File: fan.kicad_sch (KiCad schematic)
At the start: 11 parts, among them J4 Conn_01x04, U7 EMC2101

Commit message: added almost all of the feedback from NebulaMiner
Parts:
- added R?: 10K, Resistor_SMD:R_0402_1005Metric, symbol Device:R_US
- added R?: 19.3K, Resistor_SMD:R_0402_1005Metric, symbol Device:R_US
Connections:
- net FAN_TACH: now also R?.2
- net GND: now also R?.1
- new net ALERT: R?.1, R?.2
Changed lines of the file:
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@@
   (junction (at 113.665 78.105) (diameter 0) (color 0 0 0 0)
   )
+  (junction (at 74.295 108.585) (diameter 0) (color 0 0 0 0)
+  )
   (junction (at 191.77 66.04) (diameter 0) (color 0 0 0 0)
   )
@@
     (stroke (width 0) (type default) (color 0 0 0 0))
   )
+  (wire (pts (xy 74.295 105.41) (xy 74.295 108.585))
+    (stroke (width 0) (type default) (color 0 0 0 0))
+  )
   (wire (pts (xy 191.77 66.04) (xy 191.77 73.66))
     (stroke (width 0) (type default) (color 0 0 0 0))
@@
     (stroke (width 0) (type default) (color 0 0 0 0))
   )
+  (wire (pts (xy 74.295 108.585) (xy 74.295 111.125))
+    (stroke (width 0) (type default) (color 0 0 0 0))
+  )
   (wire (pts (xy 103.505 71.755) (xy 103.505 88.9))
     (stroke (width 0) (type default) (color 0 0 0 0))
@@
     (stroke (width 0) (type default) (color 0 0 0 0))
   )
+  (wire (pts (xy 67.31 108.585) (xy 74.295 108.585))
+    (stroke (width 0) (type default) (color 0 0 0 0))
+  )
   (wire (pts (xy 157.48 83.185) (xy 191.77 83.185))
     (stroke (width 0) (type default) (color 0 0 0 0))
@@
     (stroke (width 0) (type default) (color 0 0 0 0))
   )
+  (wire (pts (xy 74.295 97.79) (xy 74.295 94.615))
+    (stroke (width 0) (type default) (color 0 0 0 0))
+  )
   (wire (pts (xy 137.16 106.68) (xy 146.685 106.68))
     (stroke (width 0) (type default) (color 0 0 0 0))
@@
     (stroke (width 0) (type default) (color 0 0 0 0))
   )
+  (wire (pts (xy 74.295 94.615) (xy 85.725 94.615))
+    (stroke (width 0) (type default) (color 0 0 0 0))
+  )
+  (wire (pts (xy 74.295 118.745) (xy 74.295 127))
+    (stroke (width 0) (type default) (color 0 0 0 0))
+  )
   (text "I2C Address: 0x4C" (at 136.525 89.535 0)
     (effects (font (size 1.27 1.27)) (justify left bottom))
   )
+  (label "GND" (at 74.295 127 0)
+    (effects (font (size 1.27 1.27)) (justify left bottom))
+  )
   (label "FAN_PWM" (at 160.02 78.105 0)
     (effects (font (size 1.27 1.27)) (justify left bottom))
@@
   )
   (label "SDA" (at 162.56 75.565 0)
+    (effects (font (size 1.27 1.27)) (justify left bottom))
+  )
+  (label "FAN_TACH" (at 75.565 94.615 0)
     (effects (font (size 1.27 1.27)) (justify left bottom))
   )
@@
   )
   (hierarchical_label "TEMP_P" (shape input) (at 80.645 69.215 180)
+    (effects (font (size 1.27 1.27)) (justify right))
+  )
+  (hierarchical_label "ALERT" (shape input) (at 67.31 108.585 180)
     (effects (font (size 1.27 1.27)) (justify right))
   )
@@
     )
     (property "DK" "1292-1639-1-ND" (id 5) (at 191.77 78.74 0)
+      (effects (font (size 1.27 1.27)) hide)
+    )
+    (pin "1")
+    (pin "2")
+  )
+  (symbol (lib_id "Device:R_US") (at 74.295 101.6 180) (unit 1)
+    (in_bom yes) (on_board yes)
+    (property "Reference" "R?" (id 0) (at 77.47 100.965 0))
+    (property "Value" "10K" (id 1) (at 78.105 103.505 0))
+    (property "Footprint" "Resistor_SMD:R_0402_1005Metric" (id 2) (at 73.279 101.346 90)
+      (effects (font (size 1.27 1.27)) hide)
+    )
+    (property "Datasheet" "~" (id 3) (at 74.295 101.6 0)
+      (effects (font (size 1.27 1.27)) hide)
+    )
+    (property "DK" "YAG1346CT-ND" (id 4) (at 74.295 101.6 0)
       (effects (font (size 1.27 1.27)) hide)
     )
@@
     (pin "4")
   )
+  (symbol (lib_id "Device:R_US") (at 74.295 114.935 180) (unit 1)
+    (in_bom yes) (on_board yes)
+    (property "Reference" "R?" (id 0) (at 77.47 114.3 0))
+    (property "Value" "19.3K" (id 1) (at 79.375 116.84 0))
+    (property "Footprint" "Resistor_SMD:R_0402_1005Metric" (id 2) (at 73.279 114.681 90)
+      (effects (font (size 1.27 1.27)) hide)
+    )
+    (property "Datasheet" "~" (id 3) (at 74.295 114.935 0)
+      (effects (font (size 1.27 1.27)) hide)
+    )
+    (pin "1")
+    (pin "2")
+  )
   (symbol (lib_id "DayMiner-eagle-import:CAP0402") (at 113.665 84.455 0) (mirror y) (unit 1)

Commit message: part library cleanup
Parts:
- C32, C33: symbol DayMiner-eagle-import:CAP0402 -> Device:C
- gave numbers to parts that had none: 2
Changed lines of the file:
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@@
     (pin "1")
   )
-  (symbol (lib_id "DayMiner-eagle-import:CAP0402") (at 191.77 78.74 0) (mirror y) (unit 1)
+  (symbol (lib_id "Device:C") (at 191.77 77.47 0) (mirror y) (unit 1)
     (in_bom yes) (on_board yes)
     (property "Reference" "C33" (id 0) (at 196.215 76.2 0)
@@
       (effects (font (size 1.27 1.27)) (justify left bottom))
     )
-    (property "Footprint" "Capacitor_SMD:C_0402_1005Metric" (id 2) (at 191.77 78.74 0)
+    (property "Footprint" "Capacitor_SMD:C_0402_1005Metric" (id 2) (at 191.77 77.47 0)
       (effects (font (size 1.27 1.27)) hide)
     )
-    (property "Datasheet" "" (id 3) (at 191.77 78.74 0)
+    (property "Datasheet" "" (id 3) (at 191.77 77.47 0)
       (effects (font (size 1.27 1.27)) hide)
     )
-    (property "Value" "311-3342-1-ND" (id 4) (at 191.77 78.74 0)
+    (property "Value" "311-3342-1-ND" (id 4) (at 191.77 77.47 0)
       (effects (font (size 1.778 1.5113)) (justify left bottom) hide)
     )
-    (property "DK" "1292-1639-1-ND" (id 5) (at 191.77 78.74 0)
+    (property "DK" "1292-1639-1-ND" (id 5) (at 191.77 77.47 0)
       (effects (font (size 1.27 1.27)) hide)
     )
@@
   (symbol (lib_id "Device:R_US") (at 74.295 101.6 180) (unit 1)
     (in_bom yes) (on_board yes)
-    (property "Reference" "R?" (id 0) (at 77.47 100.965 0))
+    (property "Reference" "R24" (id 0) (at 77.47 100.965 0))
     (property "Value" "10K" (id 1) (at 78.105 103.505 0))
     (property "Footprint" "Resistor_SMD:R_0402_1005Metric" (id 2) (at 73.279 101.346 90)
@@
   (symbol (lib_id "Device:R_US") (at 74.295 114.935 180) (unit 1)
     (in_bom yes) (on_board yes)
-    (property "Reference" "R?" (id 0) (at 77.47 114.3 0))
+    (property "Reference" "R25" (id 0) (at 77.47 114.3 0))
     (property "Value" "19.3K" (id 1) (at 79.375 116.84 0))
     (property "Footprint" "Resistor_SMD:R_0402_1005Metric" (id 2) (at 73.279 114.681 90)
@@
     (pin "2")
   )
-  (symbol (lib_id "DayMiner-eagle-import:CAP0402") (at 113.665 84.455 0) (mirror y) (unit 1)
+  (symbol (lib_id "Device:C") (at 113.665 83.185 0) (mirror y) (unit 1)
     (in_bom yes) (on_board yes)
-    (property "Reference" "C32" (id 0) (at 112.141 81.534 0)
+    (property "Reference" "C32" (id 0) (at 113.03 81.28 0)
       (effects (font (size 1.27 1.27)) (justify left bottom))
     )
-    (property "Value" "470pF" (id 1) (at 112.141 86.614 0)
+    (property "Value" "470pF" (id 1) (at 113.03 86.36 0)
       (effects (font (size 1.27 1.27)) (justify left bottom))
     )
-    (property "Footprint" "Capacitor_SMD:C_0402_1005Metric" (id 2) (at 113.665 84.455 0)
+    (property "Footprint" "Capacitor_SMD:C_0402_1005Metric" (id 2) (at 113.665 83.185 0)
       (effects (font (size 1.27 1.27)) hide)
     )
-    (property "Datasheet" "" (id 3) (at 113.665 84.455 0)
+    (property "Datasheet" "" (id 3) (at 113.665 83.185 0)
       (effects (font (size 1.27 1.27)) hide)
     )
-    (property "DK" "" (id 4) (at 113.665 84.455 0)
+    (property "DK" "" (id 4) (at 113.665 83.185 0)
       (effects (font (size 1.778 1.5113)) (justify left bottom) hide)
     )

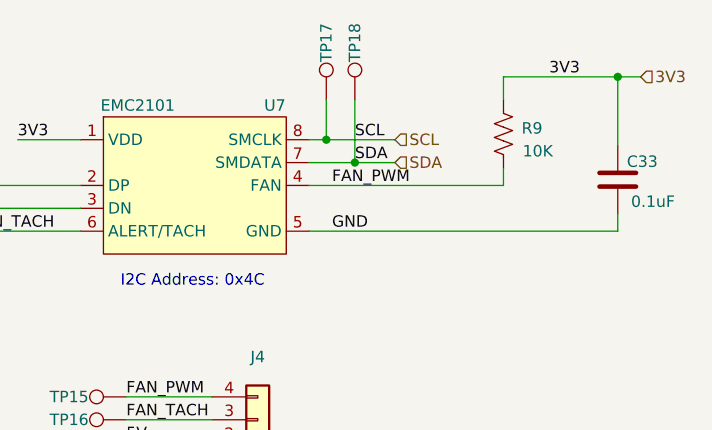
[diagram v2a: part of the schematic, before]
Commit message: more routing. fixed SDA/SCL short
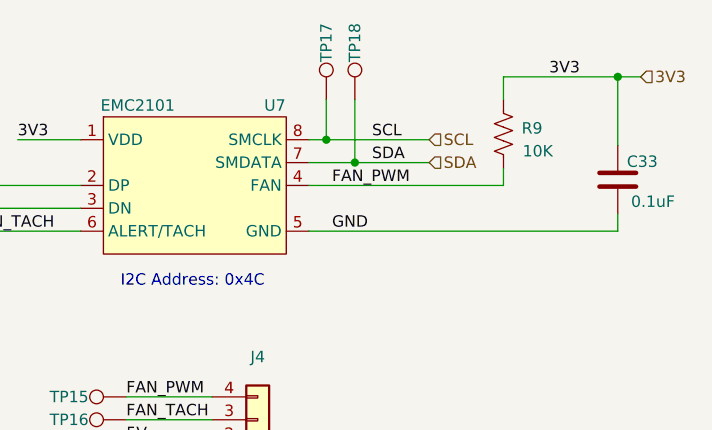
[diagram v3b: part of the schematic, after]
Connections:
- net SCL: no longer TP18.1, U7.7 (SMDATA)
- new net SDA: TP18.1, U7.7 (SMDATA)
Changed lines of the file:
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@@
     (stroke (width 0) (type default) (color 0 0 0 0))
   )
-  (wire (pts (xy 162.56 75.565) (xy 167.005 75.565))
+  (wire (pts (xy 162.56 75.565) (xy 170.815 75.565))
     (stroke (width 0) (type default) (color 0 0 0 0))
   )
@@
     (stroke (width 0) (type default) (color 0 0 0 0))
   )
-  (wire (pts (xy 159.385 73.025) (xy 167.005 73.025))
+  (wire (pts (xy 159.385 73.025) (xy 170.815 73.025))
     (stroke (width 0) (type default) (color 0 0 0 0))
   )
@@
     (effects (font (size 1.27 1.27)) (justify left bottom))
   )
-  (label "SCL" (at 162.56 73.025 0)
+  (label "SCL" (at 164.465 73.025 0)
     (effects (font (size 1.27 1.27)) (justify left bottom))
   )
@@
     (effects (font (size 1.27 1.27)) (justify left bottom))
   )
-  (label "SDA" (at 162.56 75.565 0)
+  (label "SDA" (at 164.465 75.565 0)
     (effects (font (size 1.27 1.27)) (justify left bottom))
   )
@@
     (effects (font (size 1.27 1.27)) (justify right))
   )
-  (hierarchical_label "SCL" (shape input) (at 167.005 73.025 0)
+  (hierarchical_label "SCL" (shape input) (at 170.815 73.025 0)
     (effects (font (size 1.27 1.27)) (justify left))
   )
@@
     (effects (font (size 1.27 1.27)) (justify right))
   )
-  (hierarchical_label "SDA" (shape input) (at 167.005 75.565 0)
+  (hierarchical_label "SDA" (shape input) (at 170.815 75.565 0)
     (effects (font (size 1.27 1.27)) (justify left))
   )

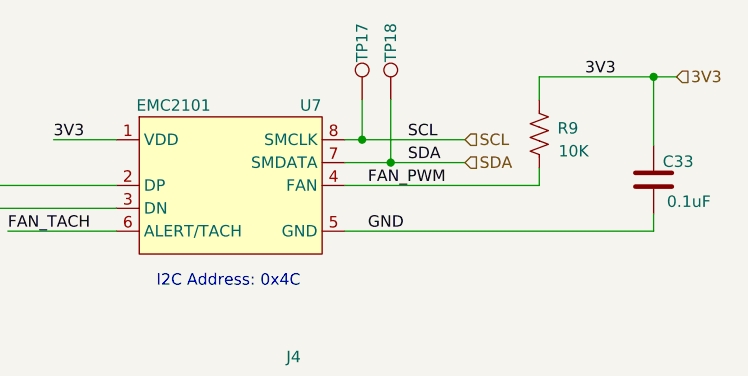
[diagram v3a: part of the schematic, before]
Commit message: lots of signals routed. much better ESP32-S3 3D model
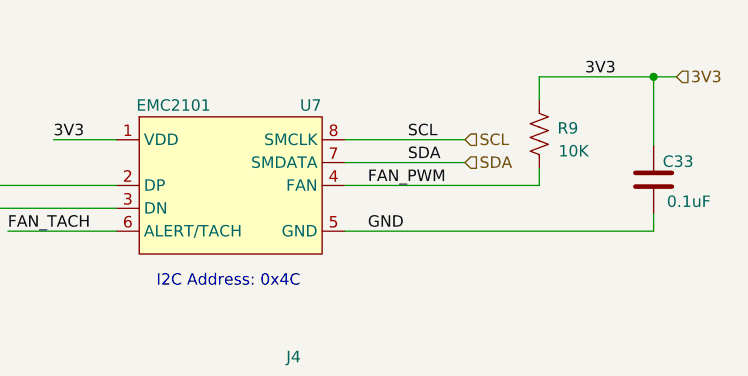
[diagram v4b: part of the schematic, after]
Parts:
- removed TP17, TP18: TestPoint, TestPoint:TestPoint_Pad_D1.5mm, symbol Connector:TestPoint
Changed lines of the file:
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@@
 (kicad_sch (version 20211123) (generator eeschema)
   (paper "A4")
-  (junction (at 162.56 75.565) (diameter 0) (color 0 0 0 0)
-  )
   (junction (at 113.665 78.105) (diameter 0) (color 0 0 0 0)
   )
@@
   (junction (at 191.77 66.04) (diameter 0) (color 0 0 0 0)
   )
-  (junction (at 159.385 73.025) (diameter 0) (color 0 0 0 0)
-  )
   (junction (at 113.665 88.9) (diameter 0) (color 0 0 0 0)
   )
-  (wire (pts (xy 157.48 73.025) (xy 159.385 73.025))
-    (stroke (width 0) (type default) (color 0 0 0 0))
-  )
-  (wire (pts (xy 159.385 68.58) (xy 159.385 73.025))
+  (wire (pts (xy 157.48 73.025) (xy 170.815 73.025))
     (stroke (width 0) (type default) (color 0 0 0 0))
   )
@@
     (stroke (width 0) (type default) (color 0 0 0 0))
   )
-  (wire (pts (xy 162.56 68.58) (xy 162.56 75.565))
-    (stroke (width 0) (type default) (color 0 0 0 0))
-  )
   (wire (pts (xy 80.645 71.755) (xy 92.075 71.755))
     (stroke (width 0) (type default) (color 0 0 0 0))
@@
     (stroke (width 0) (type default) (color 0 0 0 0))
   )
-  (wire (pts (xy 162.56 75.565) (xy 170.815 75.565))
+  (wire (pts (xy 157.48 75.565) (xy 170.815 75.565))
     (stroke (width 0) (type default) (color 0 0 0 0))
   )
@@
     (stroke (width 0) (type default) (color 0 0 0 0))
   )
-  (wire (pts (xy 159.385 73.025) (xy 170.815 73.025))
-    (stroke (width 0) (type default) (color 0 0 0 0))
-  )
   (wire (pts (xy 74.295 105.41) (xy 74.295 108.585))
     (stroke (width 0) (type default) (color 0 0 0 0))
@@
   )
   (wire (pts (xy 157.48 83.185) (xy 191.77 83.185))
-    (stroke (width 0) (type default) (color 0 0 0 0))
-  )
-  (wire (pts (xy 157.48 75.565) (xy 162.56 75.565))
     (stroke (width 0) (type default) (color 0 0 0 0))
   )
@@
     (pin "1")
     (pin "2")
-  )
-  (symbol (lib_id "Connector:TestPoint") (at 162.56 68.58 0) (mirror y) (unit 1)
-    (in_bom yes) (on_board yes)
-    (property "Reference" "TP18" (id 0) (at 162.56 62.23 90))
-    (property "Value" "TestPoint" (id 1) (at 161.2901 62.865 90)
-      (effects (font (size 1.27 1.27)) (justify left) hide)
-    )
-    (property "Footprint" "TestPoint:TestPoint_Pad_D1.5mm" (id 2) (at 157.48 68.58 0)
-      (effects (font (size 1.27 1.27)) hide)
-    )
-    (property "Datasheet" "~" (id 3) (at 157.48 68.58 0)
-      (effects (font (size 1.27 1.27)) hide)
-    )
-    (property "DNP" "T" (id 4) (at 162.56 68.58 0)
-      (effects (font (size 1.27 1.27)) hide)
-    )
-    (pin "1")
   )
   (symbol (lib_id "Connector_Generic:Conn_01x04") (at 151.765 106.68 0) (mirror x) (unit 1)
@@
     (pin "2")
   )
-  (symbol (lib_id "Connector:TestPoint") (at 159.385 68.58 0) (mirror y) (unit 1)
-    (in_bom yes) (on_board yes)
-    (property "Reference" "TP17" (id 0) (at 159.385 62.23 90))
-    (property "Value" "TestPoint" (id 1) (at 158.1151 62.865 90)
-      (effects (font (size 1.27 1.27)) (justify left) hide)
-    )
-    (property "Footprint" "TestPoint:TestPoint_Pad_D1.5mm" (id 2) (at 154.305 68.58 0)
-      (effects (font (size 1.27 1.27)) hide)
-    )
-    (property "Datasheet" "~" (id 3) (at 154.305 68.58 0)
-      (effects (font (size 1.27 1.27)) hide)
-    )
-    (property "DNP" "T" (id 4) (at 159.385 68.58 0)
-      (effects (font (size 1.27 1.27)) hide)
-    )
-    (pin "1")
-  )
   (symbol (lib_id "Device:R_US") (at 179.07 72.39 180) (unit 1)

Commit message: some DRC and BOM work
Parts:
- C32: DK (none) -> 1276-1566-1-ND
- R25: value 19.3K -> 19.1K; DK (none) -> YAG3027CT-ND
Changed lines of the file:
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@@
       (effects (font (size 1.27 1.27)) hide)
     )
-    (property "Datasheet" "" (id 3) (at 97.79 69.215 0)
+    (property "Datasheet" "~" (id 3) (at 97.79 69.215 0)
       (effects (font (size 1.27 1.27)) hide)
     )
@@
     (in_bom yes) (on_board yes)
     (property "Reference" "R25" (id 0) (at 77.47 114.3 0))
-    (property "Value" "19.3K" (id 1) (at 79.375 116.84 0))
+    (property "Value" "19.1K" (id 1) (at 79.375 116.84 0))
     (property "Footprint" "Resistor_SMD:R_0402_1005Metric" (id 2) (at 73.279 114.681 90)
       (effects (font (size 1.27 1.27)) hide)
     )
     (property "Datasheet" "~" (id 3) (at 74.295 114.935 0)
+      (effects (font (size 1.27 1.27)) hide)
+    )
+    (property "DK" "YAG3027CT-ND" (id 4) (at 74.295 114.935 0)
       (effects (font (size 1.27 1.27)) hide)
     )
@@
       (effects (font (size 1.27 1.27)) hide)
     )
-    (property "DK" "" (id 4) (at 113.665 83.185 0)
+    (property "DK" "1276-1566-1-ND" (id 4) (at 113.665 83.185 0)
       (effects (font (size 1.778 1.5113)) (justify left bottom) hide)
     )
@@
       (effects (font (size 1.27 1.27)) hide)
     )
-    (property "Datasheet" "" (id 3) (at 97.155 71.755 0)
+    (property "Datasheet" "~" (id 3) (at 97.155 71.755 0)
       (effects (font (size 1.27 1.27)) hide)
     )

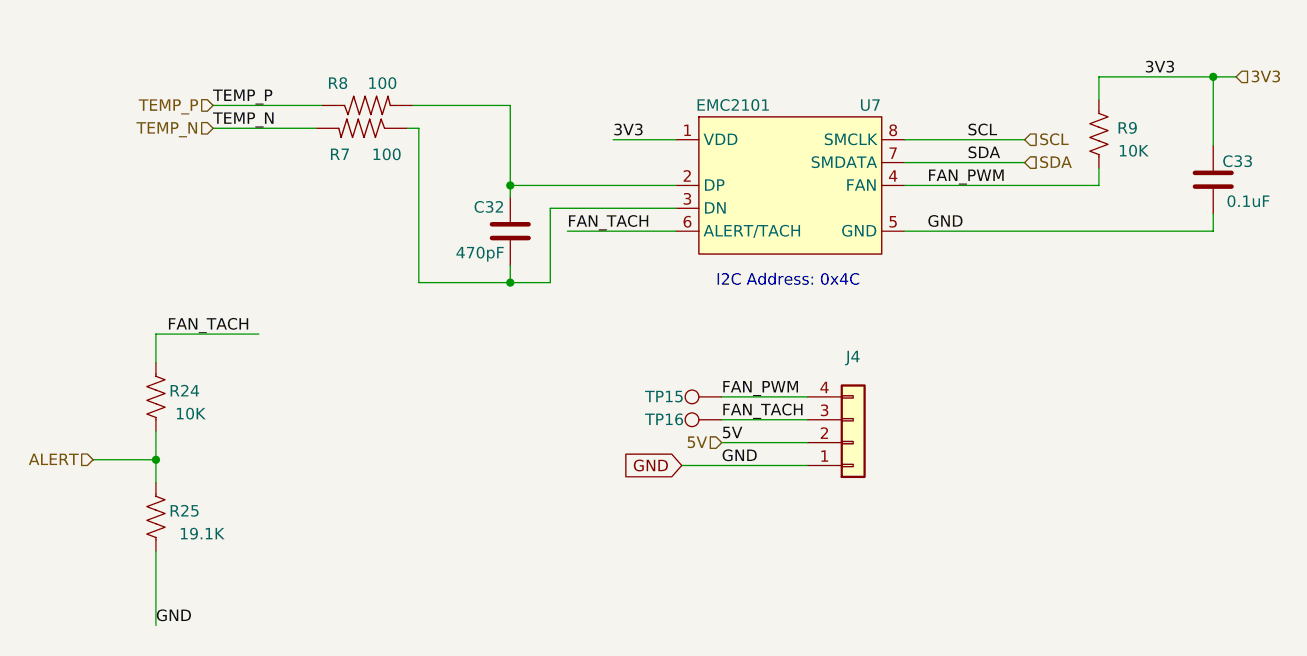
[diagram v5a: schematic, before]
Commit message: sorted out the resistor values for the DS4432. added some power filtering for the fan. created BOM
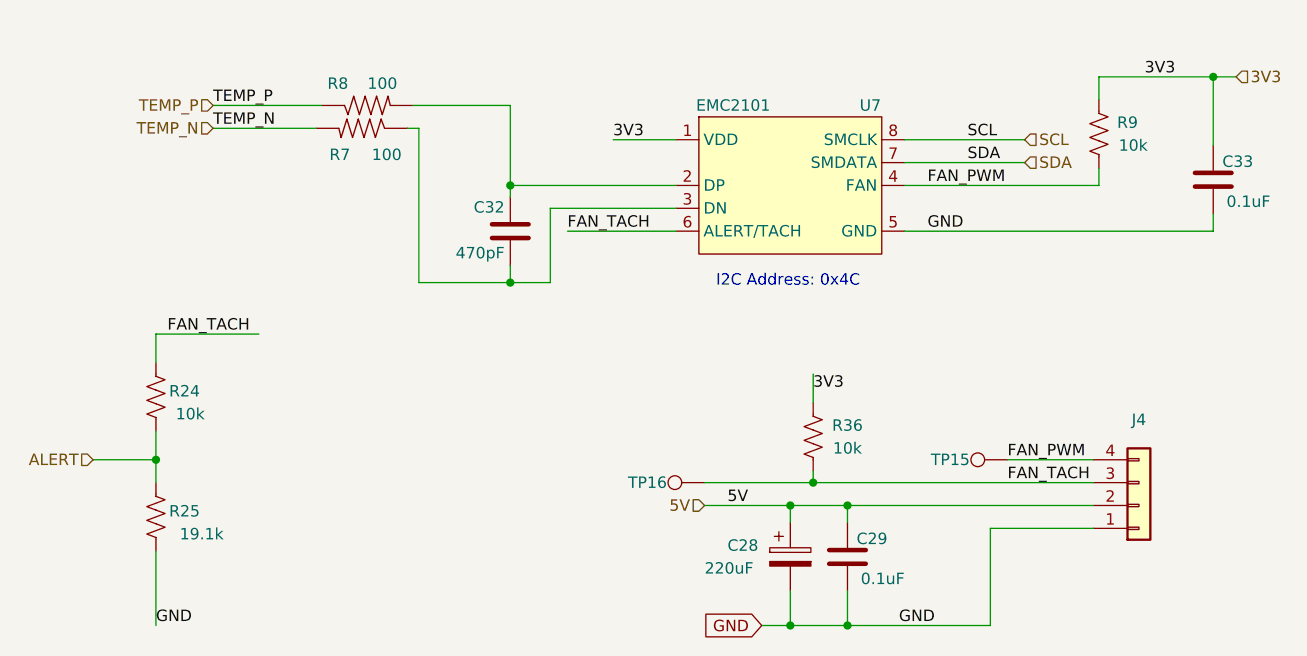
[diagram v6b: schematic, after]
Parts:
- added C28: 220uF, Capacitor_SMD:CP_Elec_6.3x7.7, symbol Device:C_Polarized
- added C29: 311-3342-1-ND, Capacitor_SMD:C_0402_1005Metric, symbol Device:C
- added R36: 10k, Resistor_SMD:R_0402_1005Metric, symbol Device:R_US
- R24, R9: value 10K -> 10k; DK YAG1346CT-ND -> 311-10KJRCT-ND
- R25: value 19.1K -> 19.1k
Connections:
- net 3V3: now also R36.2
- net 5V: now also C28.1, C29.1
- net FAN_TACH: now also R36.1
- net GND: now also C28.2, C29.2
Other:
- moved on the sheet: J4, TP15, TP16

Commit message: updated the fan connector for #21
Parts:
- J4: footprint Connector_Molex:Molex_KK-254_AE-6410-04A_1x04_P2.54mm_Vertical -> bitaxe:470531000; DK WM4202-ND -> WM4330-ND; PARTNO 0022232041 -> 0470531000
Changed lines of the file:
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@@
       (effects (font (size 1.27 1.27)) hide)
     )
-    (property "Footprint" "Connector_Molex:Molex_KK-254_AE-6410-04A_1x04_P2.54mm_Vertical" (id 2) (at 183.515 113.665 0)
+    (property "Footprint" "bitaxe:470531000" (id 2) (at 183.515 113.665 0)
       (effects (font (size 1.27 1.27)) hide)
     )
@@
       (effects (font (size 1.27 1.27)) hide)
     )
-    (property "PARTNO" "0022232041" (id 4) (at 183.515 113.665 0)
+    (property "PARTNO" "0470531000" (id 4) (at 183.515 113.665 0)
       (effects (font (size 1.27 1.27)) hide)
     )
-    (property "DK" "WM4202-ND" (id 5) (at 183.515 113.665 0)
+    (property "DK" "WM4330-ND" (id 5) (at 183.515 113.665 0)
       (effects (font (size 1.27 1.27)) hide)
     )
